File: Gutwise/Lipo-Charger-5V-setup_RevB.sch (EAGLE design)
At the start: 10 parts

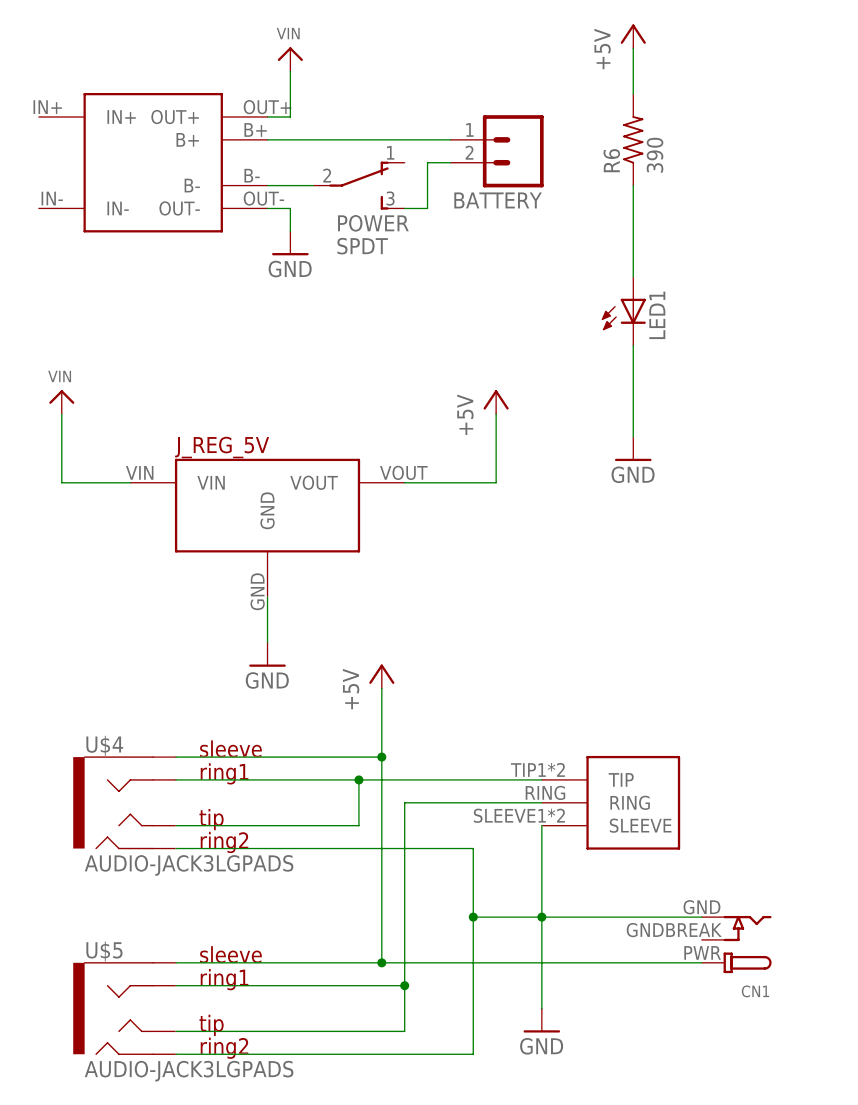
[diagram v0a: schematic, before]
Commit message: new Gutwise power board
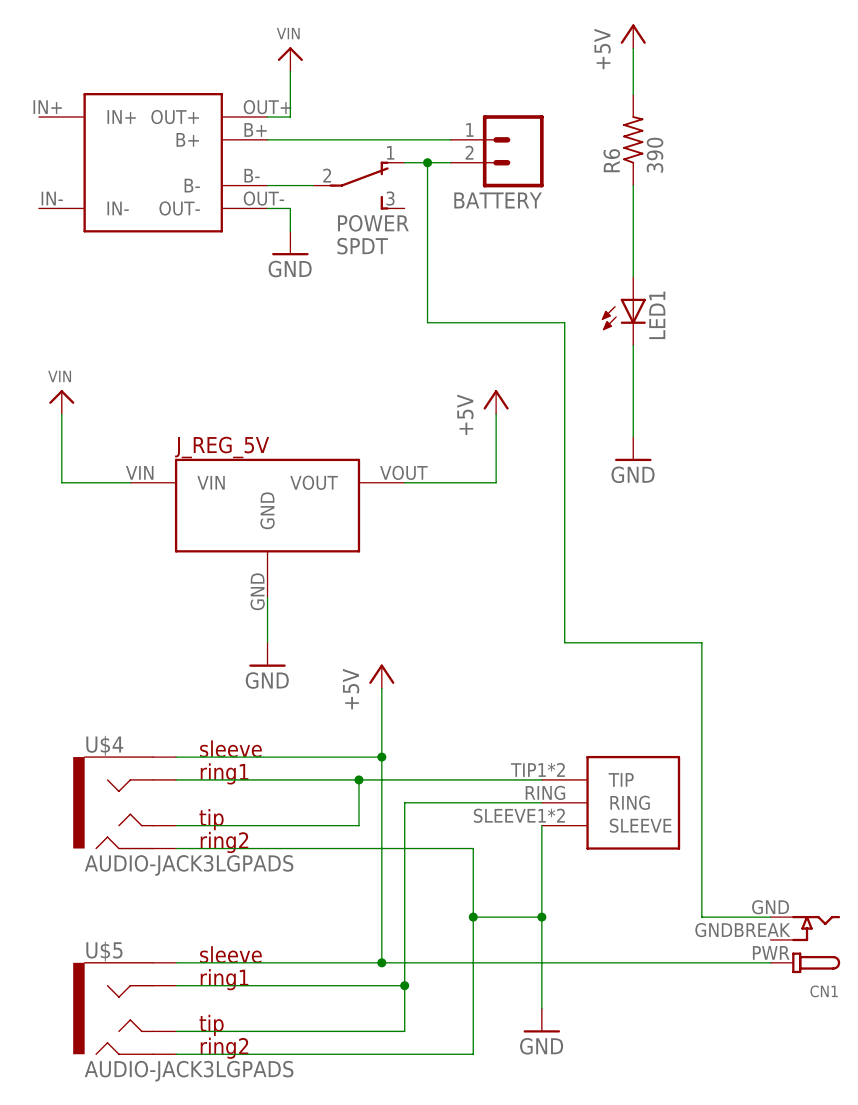
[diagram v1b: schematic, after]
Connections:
- net GND: no longer CN1.GND
- net N$1: now also CN1.GND, POWER.1; no longer POWER.3
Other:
- moved on the sheet: CN1
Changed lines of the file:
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@@
 <instance part="U$4" gate="G$1" x="-7.62" y="5.08"/>
 <instance part="U$5" gate="G$1" x="-7.62" y="-17.78"/>
-<instance part="CN1" gate="G$1" x="58.42" y="-10.16" rot="R180"/>
+<instance part="CN1" gate="G$1" x="66.04" y="-10.16" rot="R180"/>
 <instance part="P+1" gate="1" x="33.02" y="50.8"/>
 <instance part="P+2" gate="1" x="20.32" y="20.32"/>
@@
 <pinref part="AUDIO_OUT" gate="G$1" pin="SLEEVE"/>
 <wire x1="38.1" y1="2.54" x2="38.1" y2="-7.62" width="0.1524" layer="91"/>
-<pinref part="CN1" gate="G$1" pin="GND"/>
-<wire x1="38.1" y1="-7.62" x2="55.88" y2="-7.62" width="0.1524" layer="91"/>
 <wire x1="30.48" y1="-7.62" x2="38.1" y2="-7.62" width="0.1524" layer="91"/>
 <junction x="38.1" y="-7.62"/>
@@
 <wire x1="-2.54" y1="-12.7" x2="20.32" y2="-12.7" width="0.1524" layer="91"/>
 <pinref part="U$4" gate="G$1" pin="EARTH"/>
-<wire x1="20.32" y1="-12.7" x2="55.88" y2="-12.7" width="0.1524" layer="91"/>
+<wire x1="20.32" y1="-12.7" x2="63.5" y2="-12.7" width="0.1524" layer="91"/>
 <wire x1="-2.54" y1="10.16" x2="20.32" y2="10.16" width="0.1524" layer="91"/>
 <wire x1="20.32" y1="10.16" x2="20.32" y2="-12.7" width="0.1524" layer="91"/>
@@
 <segment>
 <pinref part="BATTERY" gate="G$1" pin="2"/>
+<pinref part="POWER" gate="G$1" pin="1"/>
 <wire x1="27.94" y1="76.2" x2="25.4" y2="76.2" width="0.1524" layer="91"/>
-<wire x1="25.4" y1="76.2" x2="25.4" y2="71.12" width="0.1524" layer="91"/>
-<pinref part="POWER" gate="G$1" pin="3"/>
-<wire x1="25.4" y1="71.12" x2="22.86" y2="71.12" width="0.1524" layer="91"/>
+<wire x1="25.4" y1="76.2" x2="22.86" y2="76.2" width="0.1524" layer="91"/>
+<wire x1="25.4" y1="76.2" x2="25.4" y2="58.42" width="0.1524" layer="91"/>
+<junction x="25.4" y="76.2"/>
+<wire x1="25.4" y1="58.42" x2="40.64" y2="58.42" width="0.1524" layer="91"/>
+<wire x1="40.64" y1="58.42" x2="40.64" y2="22.86" width="0.1524" layer="91"/>
+<wire x1="40.64" y1="22.86" x2="55.88" y2="22.86" width="0.1524" layer="91"/>
+<wire x1="55.88" y1="22.86" x2="55.88" y2="-7.62" width="0.1524" layer="91"/>
+<pinref part="CN1" gate="G$1" pin="GND"/>
+<wire x1="55.88" y1="-7.62" x2="63.5" y2="-7.62" width="0.1524" layer="91"/>
 </segment>
 </net>
